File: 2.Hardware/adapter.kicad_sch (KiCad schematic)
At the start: 2 parts, among them U1 LoRa, U2 LCKFP_GD32F470

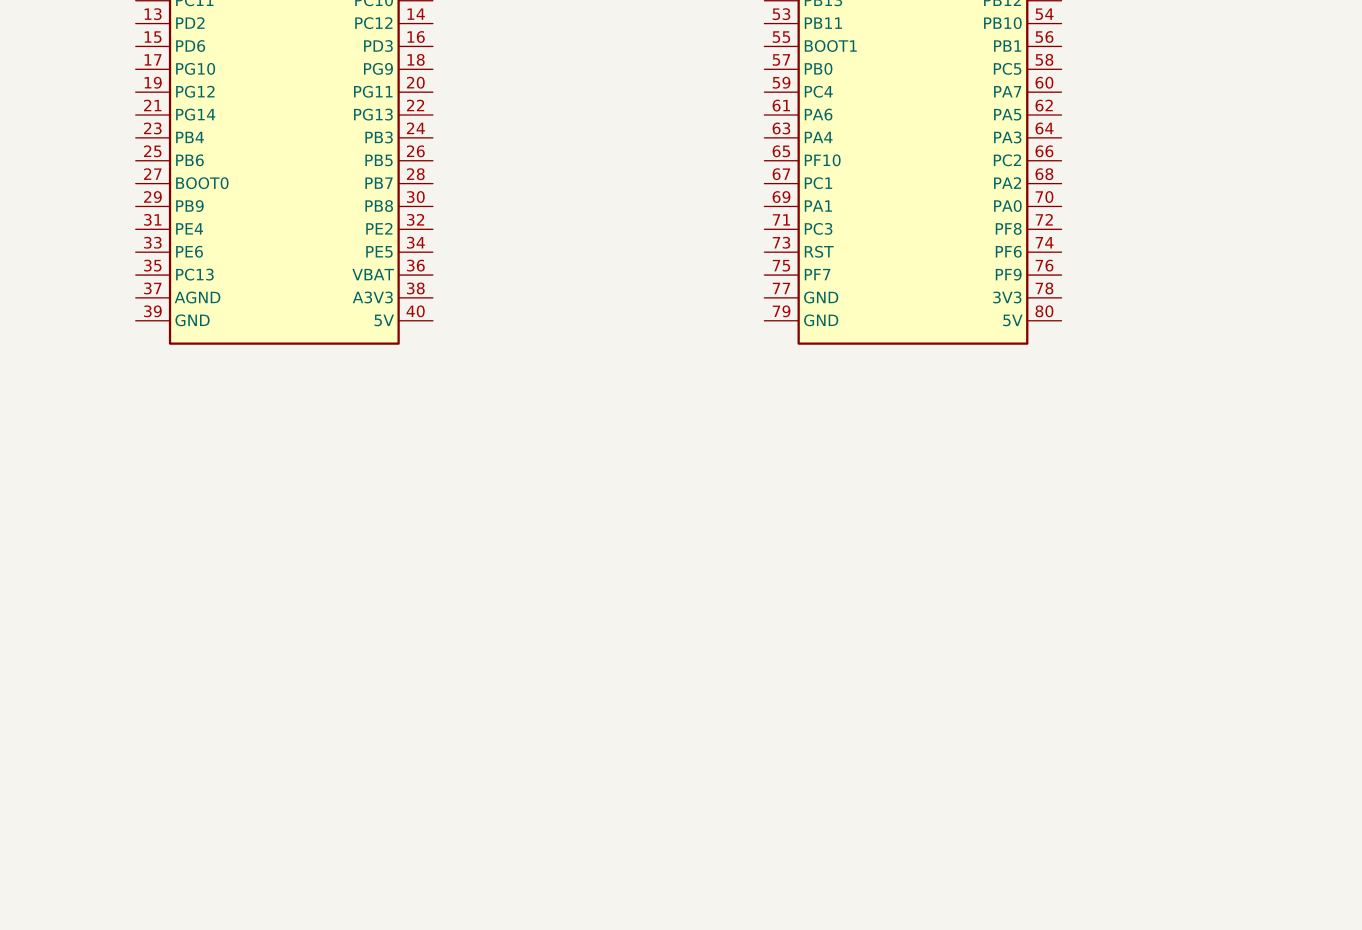
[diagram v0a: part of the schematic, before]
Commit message: add aht10 and mq2 to sch
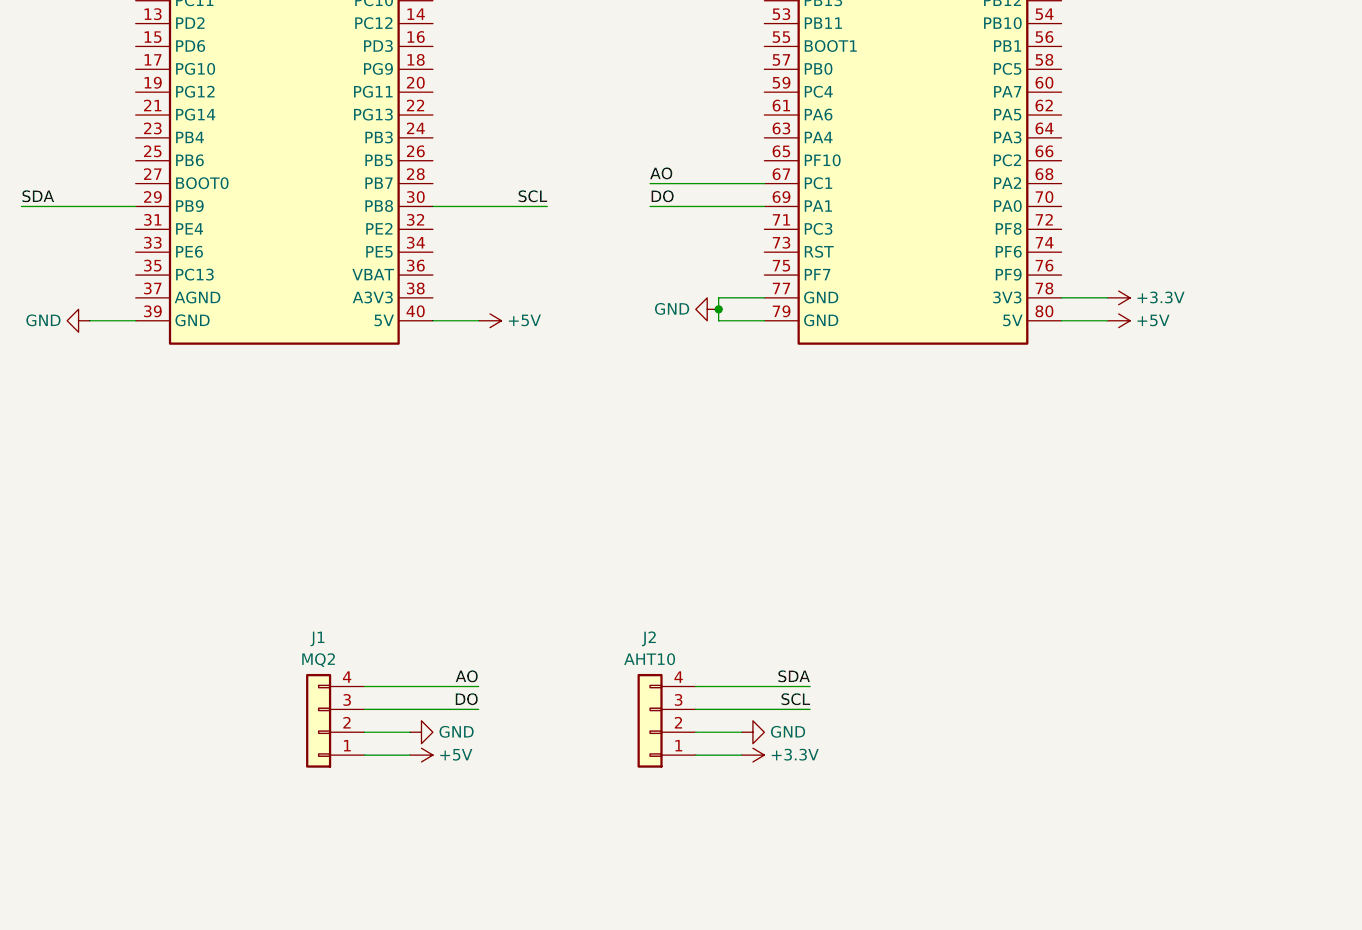
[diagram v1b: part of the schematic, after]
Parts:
- added J1: MQ2, Connector_PinSocket_2.54mm:PinSocket_1x04_P2.54mm_Vertical, symbol Connector_Generic:Conn_01x04
- added J2: AHT10, Connector_PinSocket_2.54mm:PinSocket_1x04_P2.54mm_Vertical, symbol Connector_Generic:Conn_01x04
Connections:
- net SDA: now reaches U2.29 (PB9)
- net SDA: now also J2.4 (Pin_4)
- net SCL: now reaches U2.30 (PB8)
- net SCL: now also J2.3 (Pin_3)
- net GND: now reaches U2.39 (GND)
- net GND: now also U2.77 (GND), U2.79 (GND), J1.2 (Pin_2), J2.2 (Pin_2)
- net +5V: now reaches U2.40 (5V)
- net +5V: now also U2.80 (5V), J1.1 (Pin_1)
- net AO: now reaches U2.67 (PC1)
- net AO: now also J1.4 (Pin_4)
- net DO: now reaches U2.69 (PA1)
- net DO: now also J1.3 (Pin_3)
- net +3.3V: now reaches U2.78 (3V3)
- net +3.3V: now also J2.1 (Pin_1)

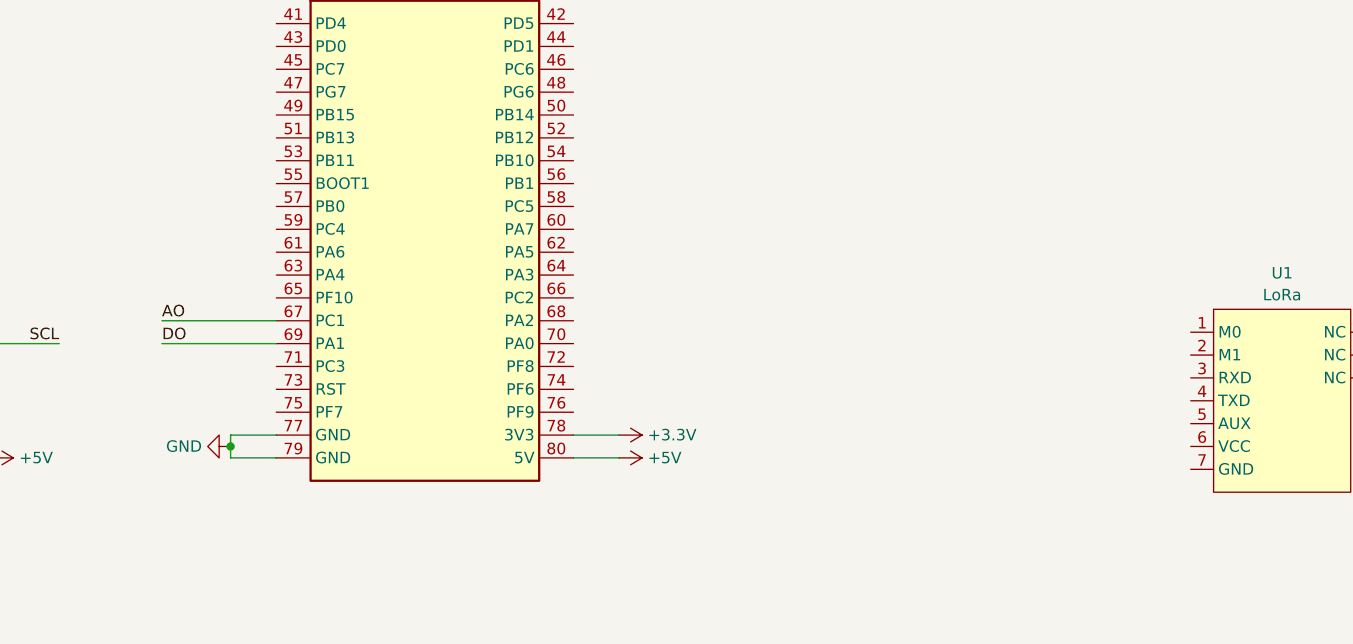
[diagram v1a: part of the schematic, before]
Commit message: link lora to  gd32
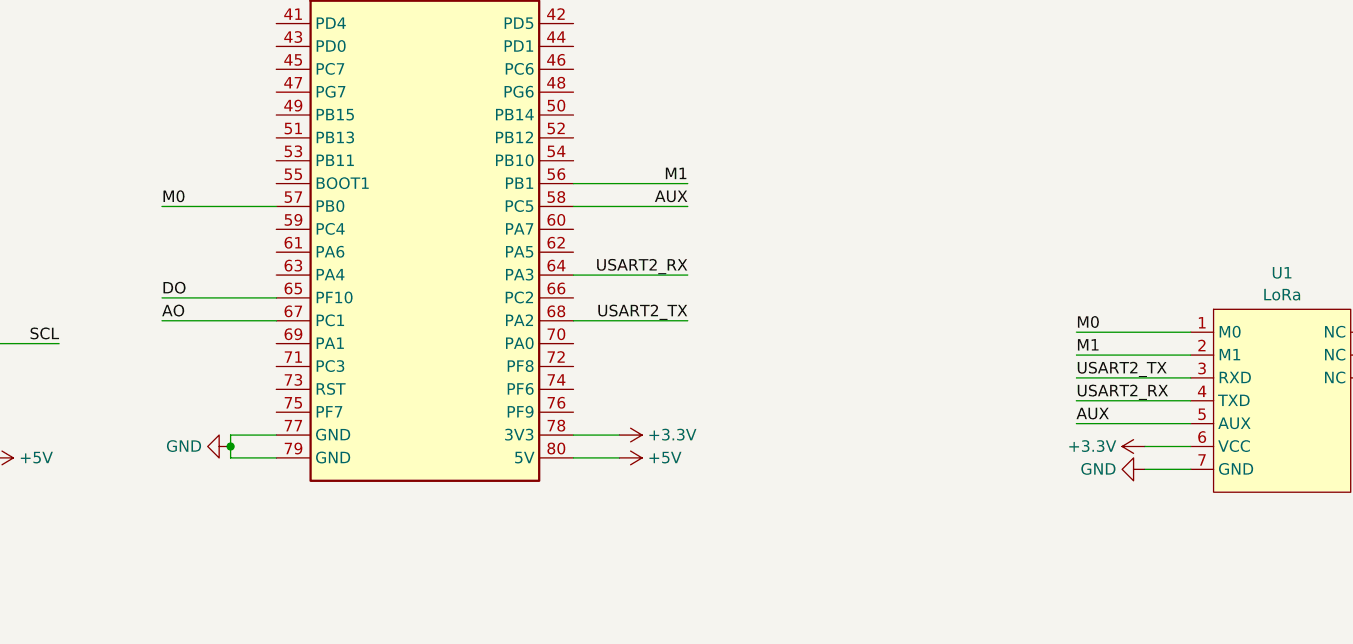
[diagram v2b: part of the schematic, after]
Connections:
- net +3.3V: now also U1.6 (VCC)
- net DO: now also U2.65 (PF10); no longer U2.69 (PA1)
- net GND: now also U1.7 (GND)
- net M0: now reaches U1.1 (M0)
- net M0: now also U2.57 (PB0)
- net M1: now reaches U1.2 (M1)
- net M1: now also U2.56 (PB1)
- net USART2_TX: now reaches U1.3 (RXD)
- net USART2_TX: now also U2.68 (PA2)
- net USART2_RX: now reaches U1.4 (TXD)
- net USART2_RX: now also U2.64 (PA3)
- net AUX: now reaches U1.5 (AUX)
- net AUX: now also U2.58 (PC5)

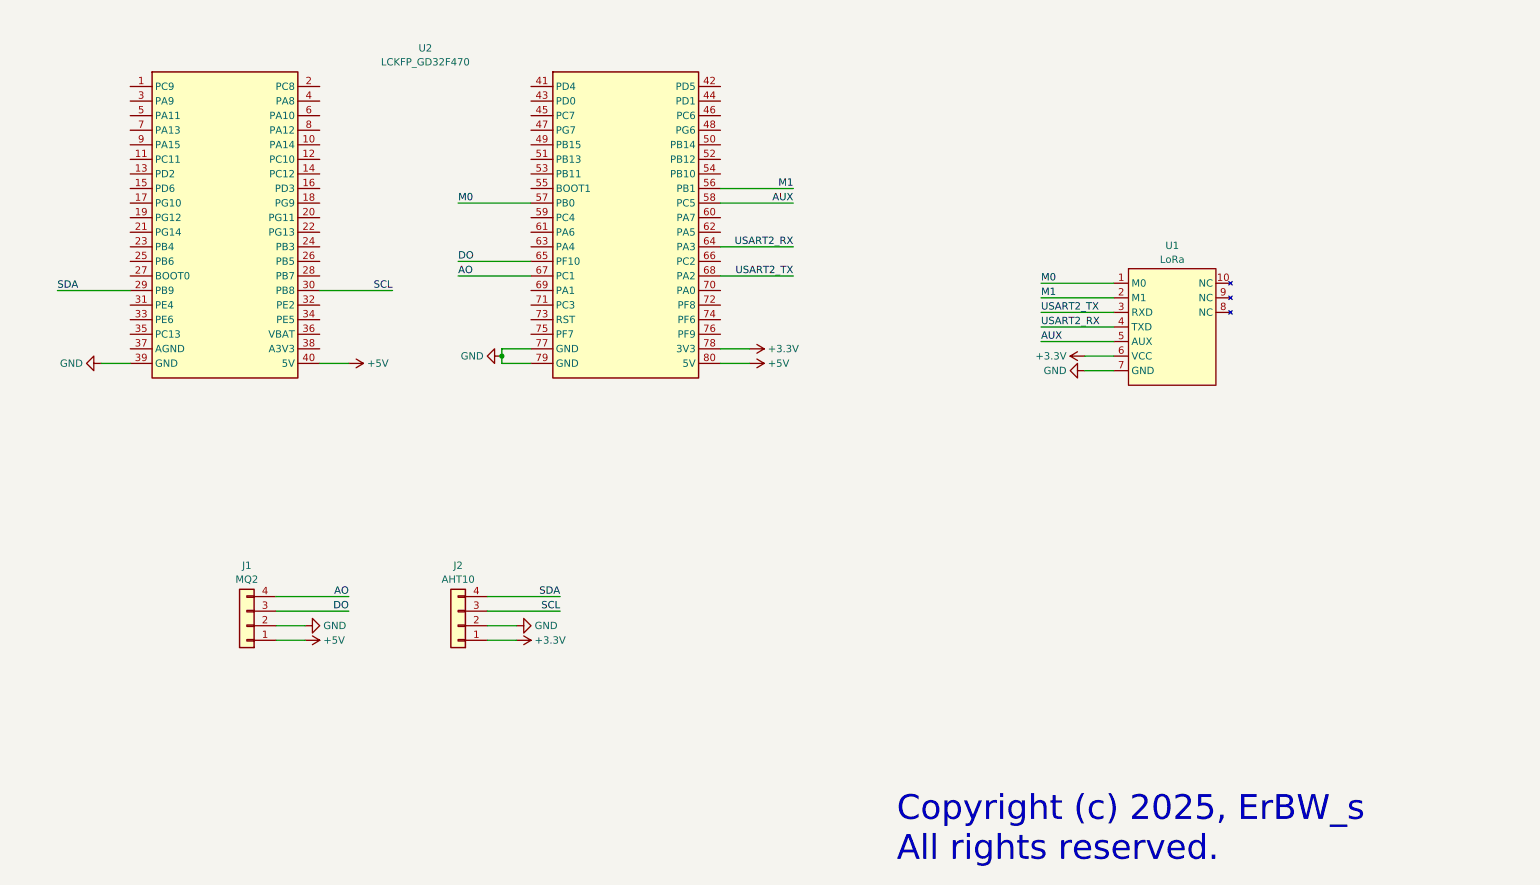
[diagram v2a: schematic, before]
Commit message: add air700e to project
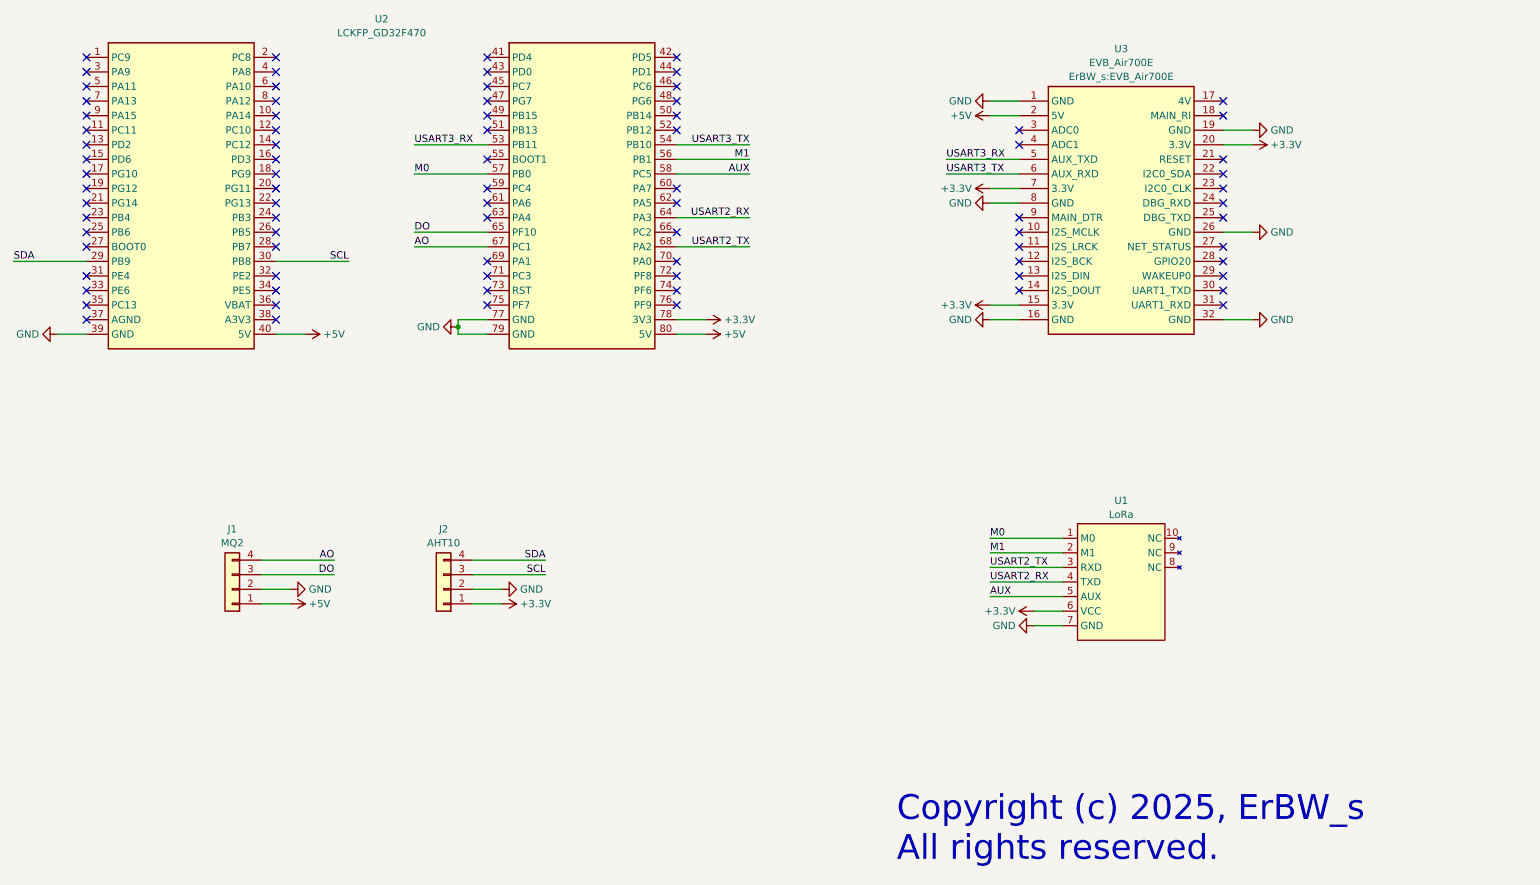
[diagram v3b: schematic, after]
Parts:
- added U3: EVB_Air700E, ErBW_s:EVB_Air700E, symbol ErBW_s:EVB_Air700E
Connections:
- net +3.3V: now also U3.15 (3.3V), U3.20 (3.3V), U3.7 (3.3V)
- net +5V: now also U3.2 (5V)
- net GND: now also U3.1 (GND), U3.16 (GND), U3.19 (GND), U3.26 (GND), U3.32 (GND), U3.8 (GND)
- net USART3_RX: now reaches U2.53 (PB11)
- net USART3_RX: now also U3.5 (AUX_TXD)
- net USART3_TX: now reaches U2.54 (PB10)
- net USART3_TX: now also U3.6 (AUX_RXD)
- no-connect marks 0 -> 83
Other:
- moved on the sheet: J1, J2, U1, U2
